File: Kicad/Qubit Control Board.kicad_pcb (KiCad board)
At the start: 6 copper layers, 144 x 89.5 mm, 131 parts, among them J1 USB_C_Receptacle_PowerOnly_6P, J2 CLK_Pins, J3 Idata, J4 Qdata, J5 SPIdata, J6 SMA, U2 TRF372017IRGZR, U3 LT1963AxST-3.3, U4 LT1963AxST-1.8, U5 SN65LVDS1DBV, U6 AD9743BCPZ, Y1 SiT8008xx-3x-xxN, Y2 CVHD-950-100.000

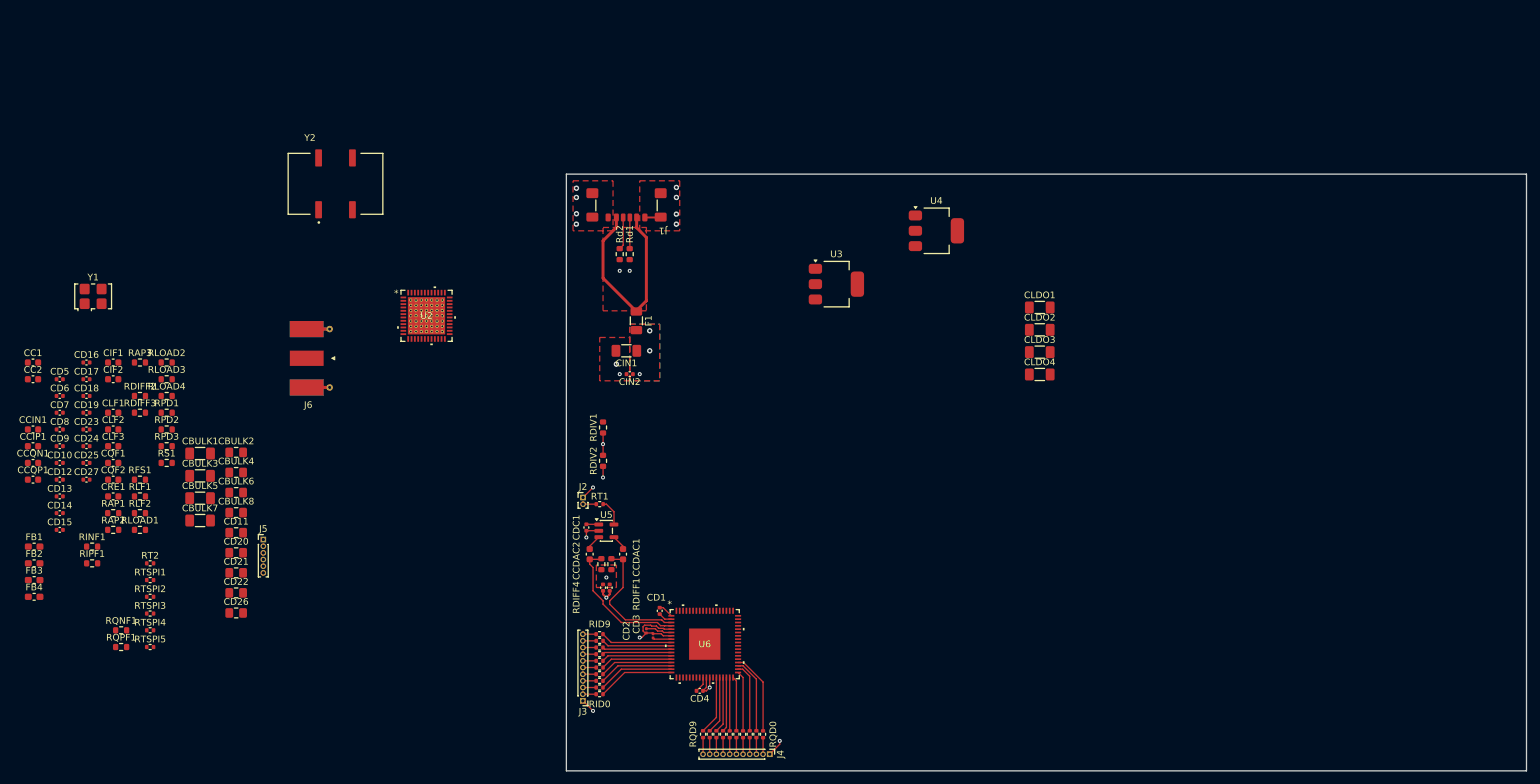
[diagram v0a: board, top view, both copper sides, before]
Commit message: re did diff clock for DAC
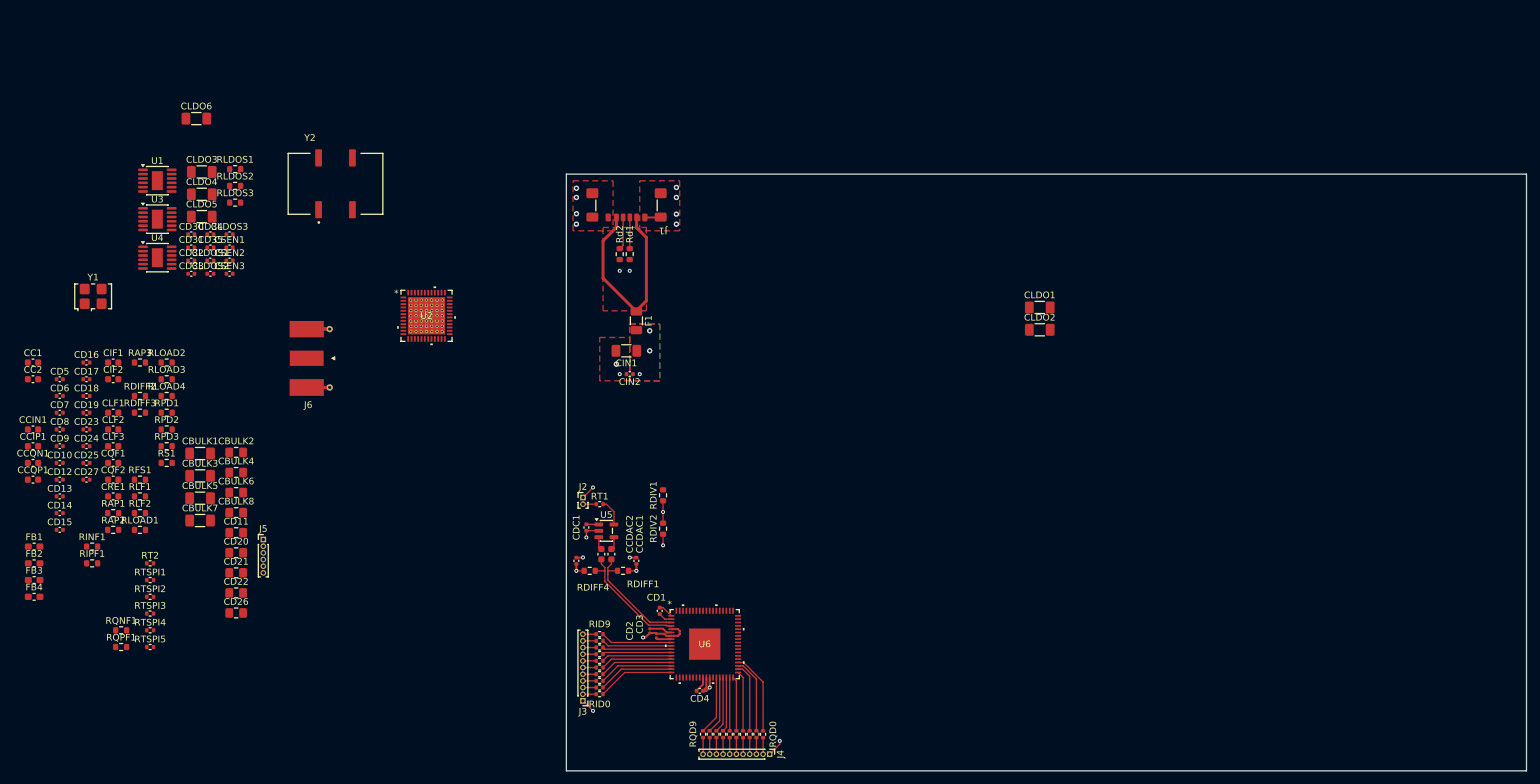
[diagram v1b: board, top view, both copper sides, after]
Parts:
- added CD30: 100n, Capacitor_SMD:C_0402_1005Metric, F.Cu at (50.2, 37.0)
- added CD31: 100n, Capacitor_SMD:C_0402_1005Metric, F.Cu at (50.2, 39.0)
- added CD32: 100n, Capacitor_SMD:C_0402_1005Metric, F.Cu at (50.2, 41.0)
- added CD33: 100n, Capacitor_SMD:C_0402_1005Metric, F.Cu at (50.2, 42.9)
- added CD34: 100n, Capacitor_SMD:C_0402_1005Metric, F.Cu at (53.1, 37.0)
- added CD35: 100n, Capacitor_SMD:C_0402_1005Metric, F.Cu at (53.1, 39.0)
- added CLDO5: 10u, Capacitor_SMD:C_1206_3216Metric_Pad1.33x1.80mm_HandSolder, F.Cu at (51.8, 34.4)
- added CLDO6: 10u, Capacitor_SMD:C_1206_3216Metric_Pad1.33x1.80mm_HandSolder, F.Cu at (51.0, 19.7)
- added CLDOS1: 470n, Capacitor_SMD:C_0402_1005Metric, F.Cu at (53.1, 41.0)
- added CLDOS2: 470n, Capacitor_SMD:C_0402_1005Metric, F.Cu at (53.1, 42.9)
- added CLDOS3: 470n, Capacitor_SMD:C_0402_1005Metric, F.Cu at (56.0, 37.0)
- added CSEN1: 100n, Capacitor_SMD:C_0402_1005Metric, F.Cu at (56.0, 39.0)
- added CSEN2: 100n, Capacitor_SMD:C_0402_1005Metric, F.Cu at (56.0, 41.0)
- added CSEN3: 100n, Capacitor_SMD:C_0402_1005Metric, F.Cu at (56.0, 42.9)
- added RLDOS1: 33.2k, Resistor_SMD:R_0603_1608Metric, F.Cu at (56.8, 27.3)
- added RLDOS2: 33.2k, Resistor_SMD:R_0603_1608Metric, F.Cu at (56.8, 29.8)
- added RLDOS3: 17.8k, Resistor_SMD:R_0603_1608Metric, F.Cu at (56.8, 32.3)
- added U1: LT3045xMSE, Package_SO:MSOP-12-1EP_3x4.039mm_P0.65mm_EP1.651x2.845mm, F.Cu at (45.2, 29.0)
- U3: value LT1963AxST-3.3 -> LT3045xMSE; footprint Package_TO_SOT_SMD:SOT-223-3_TabPin2 -> Package_SO:MSOP-12-1EP_3x4.039mm_P0.65mm_EP1.651x2.845mm
- U4: value LT1963AxST-1.8 -> LT3045xMSE; footprint Package_TO_SOT_SMD:SOT-223-3_TabPin2 -> Package_SO:MSOP-12-1EP_3x4.039mm_P0.65mm_EP1.651x2.845mm
- moved CLDO3 128.6 mm to (51.8, 27.7)
- moved CLDO4 128.6 mm to (51.8, 31.0)
- moved U4 116.9 mm to (45.2, 40.5)
- moved U3 102.3 mm to (45.2, 34.8)
- moved RDIV1 13.6 mm to (121.0, 76.2)
- moved RDIV2 13.6 mm to (121.0, 81.2)
- moved CD28 5.67 mm to (108.0, 86.0), turned to -90 degrees
- moved CD29 5.67 mm to (117.0, 86.0), turned to -90 degrees
- moved RDIFF1 2.02 mm to (115.0, 87.5), turned to 180 degrees
- moved RDIFF4 2.02 mm to (110.0, 87.5), turned to 180 degrees
- moved CCDAC1 1.75 mm to (113.2, 85.0)
- moved CCDAC2 1.75 mm to (111.8, 85.0)
- moved CD2 0.50 mm to (119.0, 96.5)
- moved CD3 0.50 mm to (120.0, 97.2)
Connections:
- CBULK3 pad 1: +3.3V -> +3.3V-A
- CBULK4 pad 1: +3.3V -> +3.3V-A
- CBULK7 pad 1: +3.3V -> +3.3V-B
- CBULK8 pad 1: +3.3V -> +3.3V-B
- CD10 pad 2: +3.3V -> +3.3V-B
- CD11 pad 2: +3.3V -> +3.3V-B
- CD4 pad 2: +3.3V -> +3.3V-A
- CD6 pad 2: +3.3V -> +3.3V-A
- CD7 pad 2: +3.3V -> +3.3V-A
- CD8 pad 2: +3.3V -> +3.3V-A
- CD9 pad 2: +3.3V -> +3.3V-A
- CDC1 pad 1: +3.3V -> +3.3V-A
- CLDO2 pad 1: +3.3V -> +5V
- CLDO4 pad 1: +1.8V -> +5V
- FB2 pad 1: +3.3V -> +3.3V-B
- FB3 pad 1: +3.3V -> +3.3V-B
- FB4 pad 1: +3.3V -> +3.3V-B
- U3 pad 2: GND -> +5V
- U3 pad 3: +3.3V -> +5V
- U4 pad 2: GND -> +5V
- U4 pad 3: +1.8V -> +5V
- U5 pad 1: +3.3V -> +3.3V-A
- U6 pad 27: +3.3V -> +3.3V-A
- U6 pad 50: +3.3V -> +3.3V-A
- U6 pad 53: +3.3V -> +3.3V-A
- U6 pad 56: +3.3V -> +3.3V-A
- U6 pad 57: +3.3V -> +3.3V-A
- U6 pad 71: +3.3V -> +3.3V-A
- U6 pad 72: +3.3V -> +3.3V-A
- Y2 pad 1: +3.3V -> +3.3V-B
- Y2 pad 4: +3.3V -> +3.3V-B
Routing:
- net Net-(CD28-Pad2): track 3.35 -> 21.8 mm, vias 2 -> 3
- net +3.3V-A: track 0.00 -> 4.28 mm
- net +3.3V: track 4.28 -> 0.00 mm
- net GND: track 35.1 -> 31.6 mm, vias 20 -> 21
- net /CLKN: track 21.0 -> 17.8 mm
- net /CLKP: track 19.7 -> 17.0 mm
- net +1.8V: track 9.05 -> 8.05 mm
- net Net-(U5-Z): track 2.34 -> 1.83 mm
- net Net-(U5-Y): track 2.34 -> 1.83 mm
- added copper zone on In2.Cu, net Net-(CD28-Pad2)
- removed copper zone on F.Cu, net Net-(CD28-Pad2)

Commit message: diff clock edits
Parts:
- moved CCDAC1 4.00 mm to (113.1, 89.0)
- moved CCDAC2 4.00 mm to (111.6, 89.0)
- moved CD28 4.00 mm to (107.8, 90.0)
- moved CD29 4.00 mm to (116.8, 90.0)
- moved CDC1 4.00 mm to (109.3, 85.0)
- moved J2 4.00 mm to (108.8, 80.5)
- moved RDIFF1 4.00 mm to (114.8, 91.5)
- moved RDIFF4 4.00 mm to (109.8, 91.5)
- moved RDIV1 4.00 mm to (120.8, 80.2)
- moved RDIV2 4.00 mm to (120.8, 85.2)
- moved RT1 4.00 mm to (111.3, 81.5)
- moved U5 4.00 mm to (112.3, 85.5)
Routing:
- net /CLKP: track 17.0 -> 14.3 mm
- net /CLKN: track 17.8 -> 15.1 mm

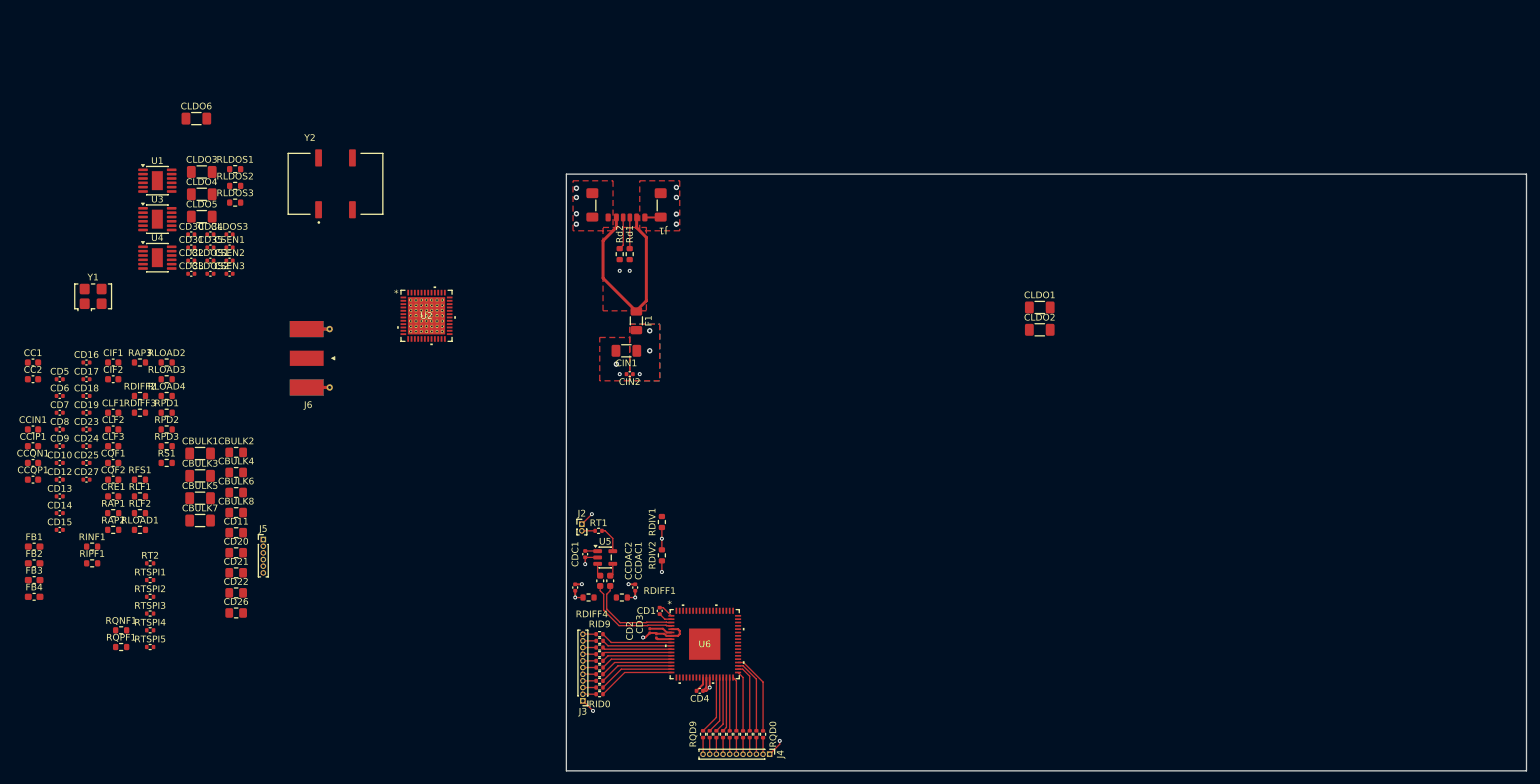
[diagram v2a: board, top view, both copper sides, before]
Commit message: started on 1.8V LDO
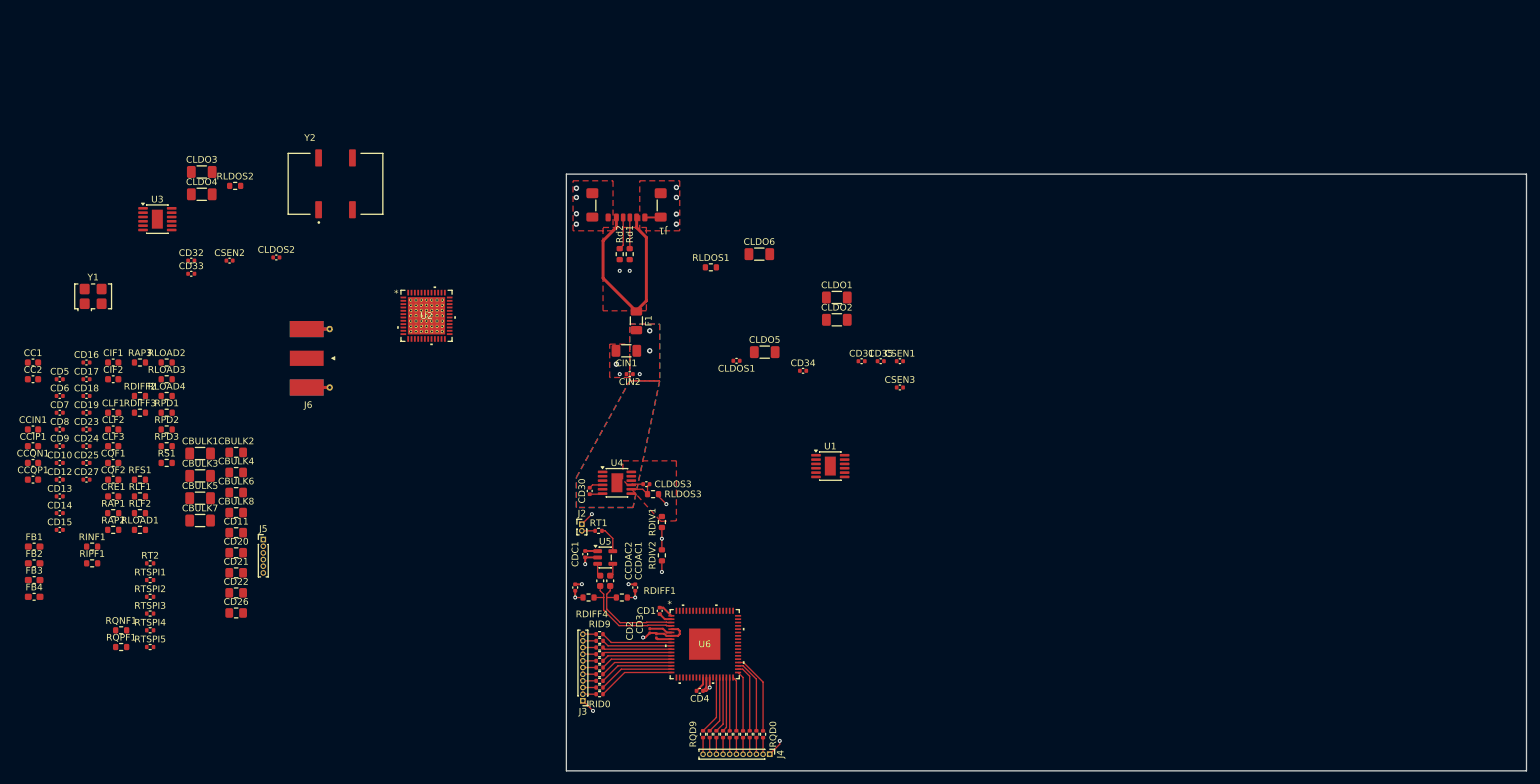
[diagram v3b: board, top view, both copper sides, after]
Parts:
- moved U1 109.6 mm to (146.1, 71.8)
- moved CSEN1 102.0 mm to (156.5, 56.1)
- moved CSEN3 102.0 mm to (156.5, 60.0)
- moved CD31 102.0 mm to (150.8, 56.1)
- moved CD35 102.0 mm to (153.7, 56.1)
- moved CD34 91.2 mm to (142.0, 57.5)
- moved CLDO5 86.8 mm to (136.2, 54.7)
- moved CLDO6 86.8 mm to (135.4, 40.0)
- moved CLDOS1 80.3 mm to (132.0, 56.0), turned to 180 degrees
- moved U4 76.8 mm to (114.1, 74.3)
- moved RLDOS3 76.4 mm to (119.5, 76.0), turned to 180 degrees
- moved CLDOS3 72.9 mm to (118.5, 74.5)
- moved RLDOS1 72.9 mm to (128.2, 42.0)
- moved CD30 71.1 mm to (110.0, 75.5), turned to 90 degrees
- moved CLDO1 30.5 mm to (147.1, 46.5)
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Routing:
- net GND: track 31.6 -> 37.4 mm, vias 21 -> 22
- net Net-(U4-SET): track 0.00 -> 4.37 mm
- net +5V: track 0.00 -> 2.11 mm
- net /CLKP: track 14.3 -> 15.7 mm
- net /CLKN: track 15.1 -> 16.5 mm
- added copper zone on F.Cu, net +1.8V

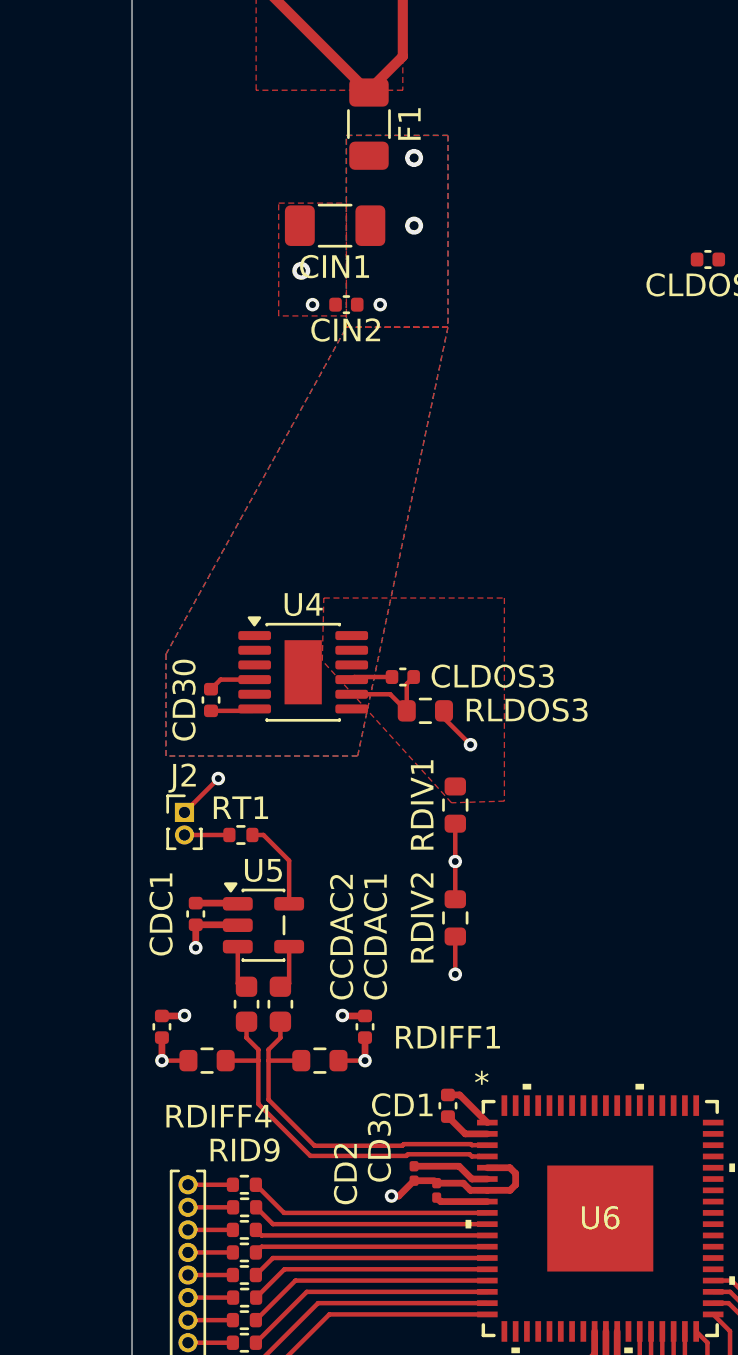
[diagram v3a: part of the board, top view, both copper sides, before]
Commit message: 1.8V LDO
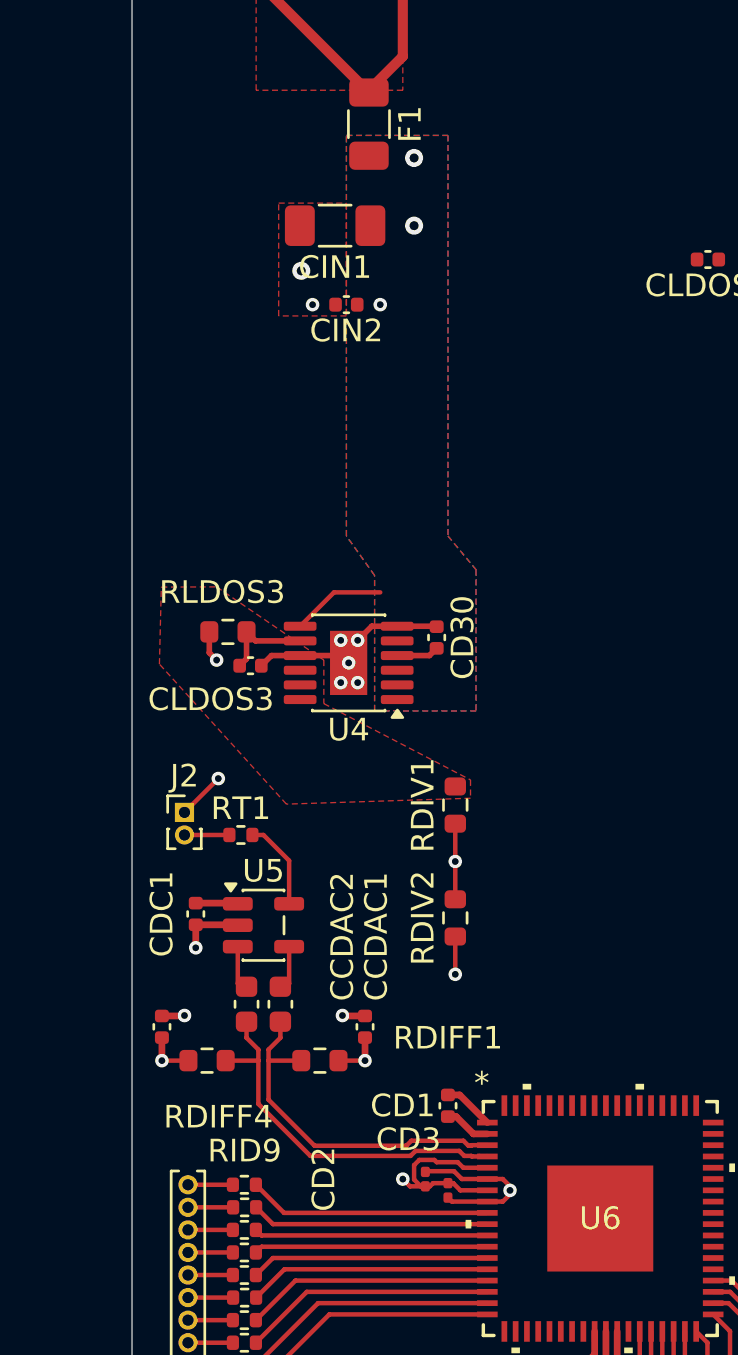
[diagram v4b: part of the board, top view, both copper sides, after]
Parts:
- moved CD30 10.4 mm to (120.0, 72.8), turned to -90 degrees
- moved RLDOS3 9.42 mm to (110.8, 72.5), turned to 0 degrees
- moved CLDOS3 6.77 mm to (111.8, 74.0), turned to 180 degrees
- moved U4 2.06 mm to (116.1, 73.9), turned to 180 degrees
- moved CD2 0.56 mm to (119.5, 96.8)
- moved CD3 0.50 mm to (120.5, 97.2)
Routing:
- net GND: track 37.4 -> 43.3 mm, vias 22 -> 27
- net +5V: track 2.11 -> 6.05 mm
- net +1.8V: track 8.05 -> 9.61 mm, vias 0 -> 1
- added copper zone on In4.Cu, net +1.8V
